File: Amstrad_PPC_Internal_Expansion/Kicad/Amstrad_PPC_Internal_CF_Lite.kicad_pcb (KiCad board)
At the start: 2 copper layers, 120 x 205 mm, 36 parts, among them J1 Amstrad_PPC_ISA_Connector_B, J2 Amstrad_PPC_ISA_Connector_A, J3 CONN_CF_CARD, J4 Conn_01x02, SW1 Switch_DIP_4_Positions, SW2 Switch_DIP_8_Positions, U1 74HCT244, U2 74HCT244, U3 74HCT688, U4 74LS32, U5 74HCT04, U6 74HCT688, U7 28C256

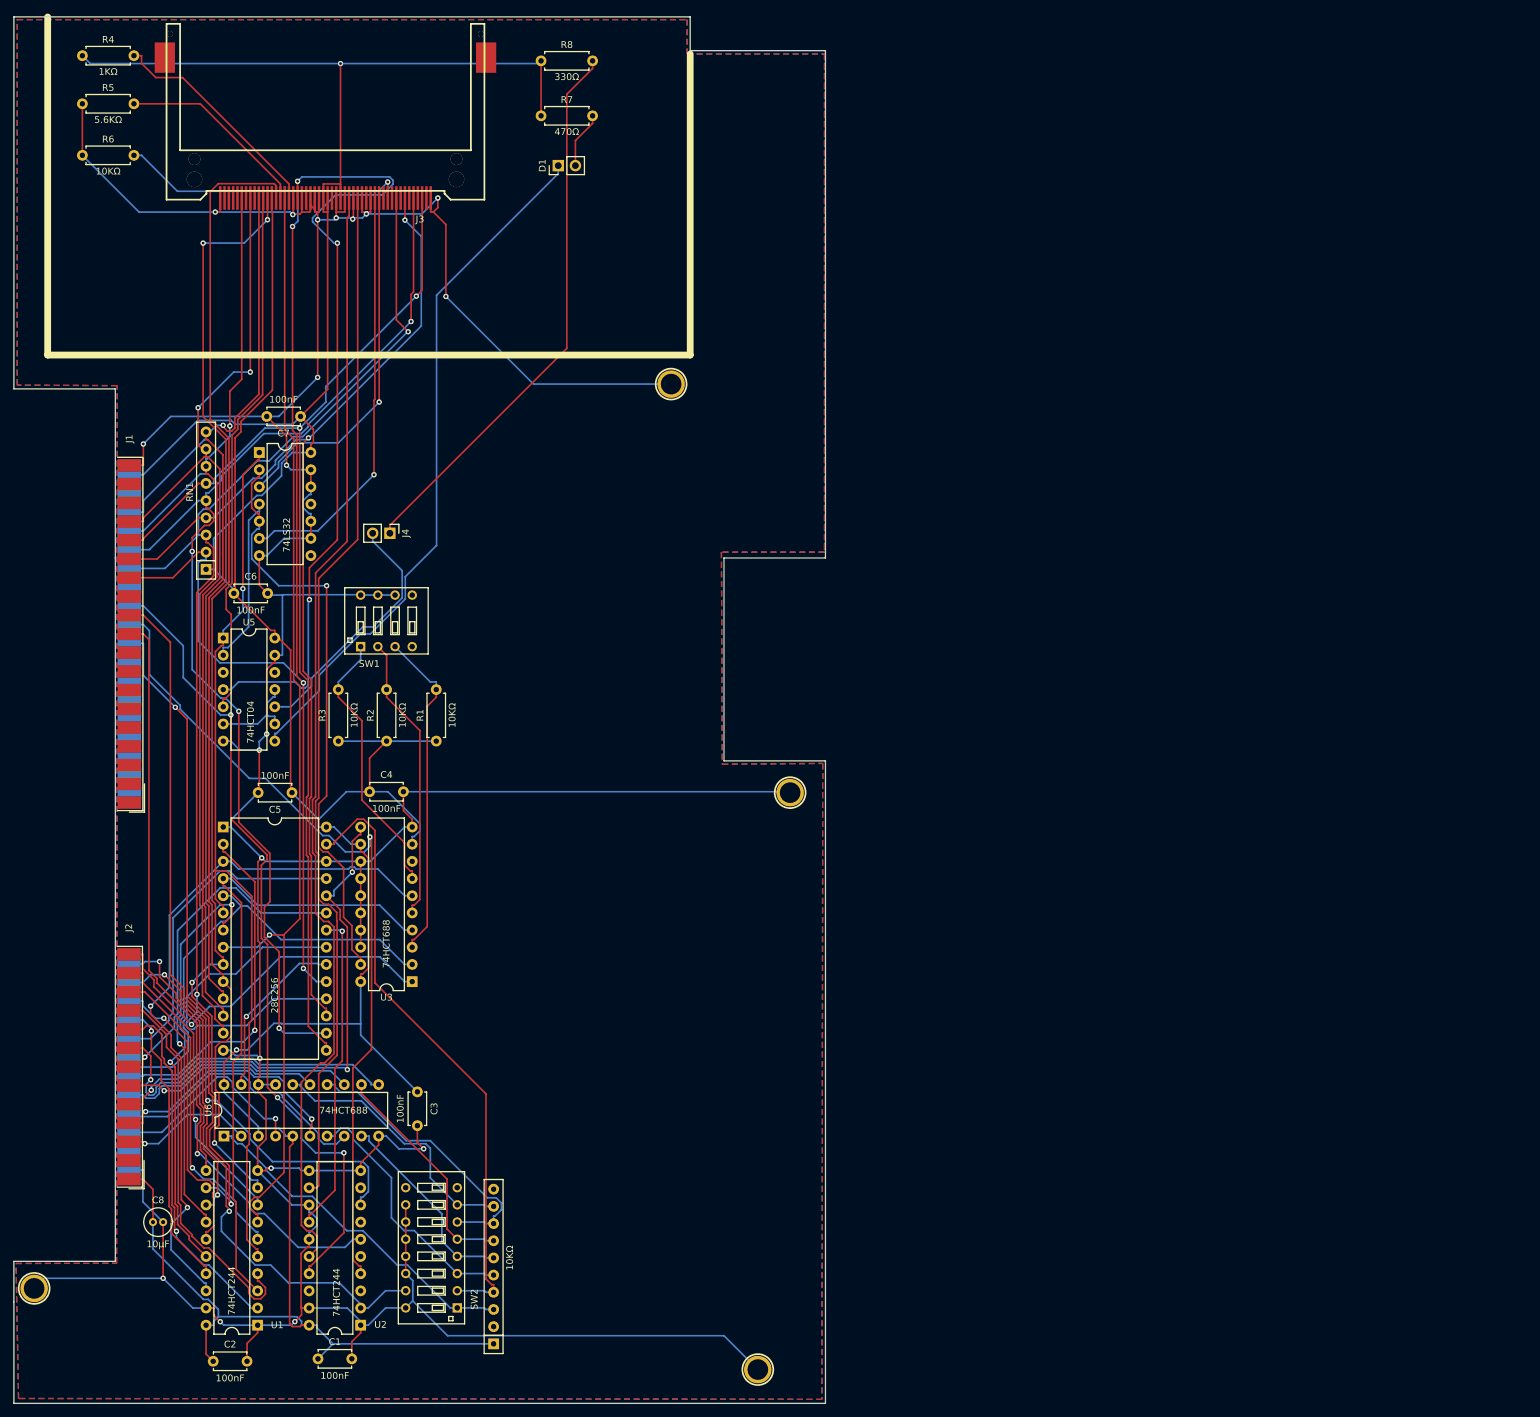
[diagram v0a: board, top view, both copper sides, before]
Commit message: Starting again ... initial schematic cleanup
Schematic is now cleaned up, no errors
Next will be PCB layout
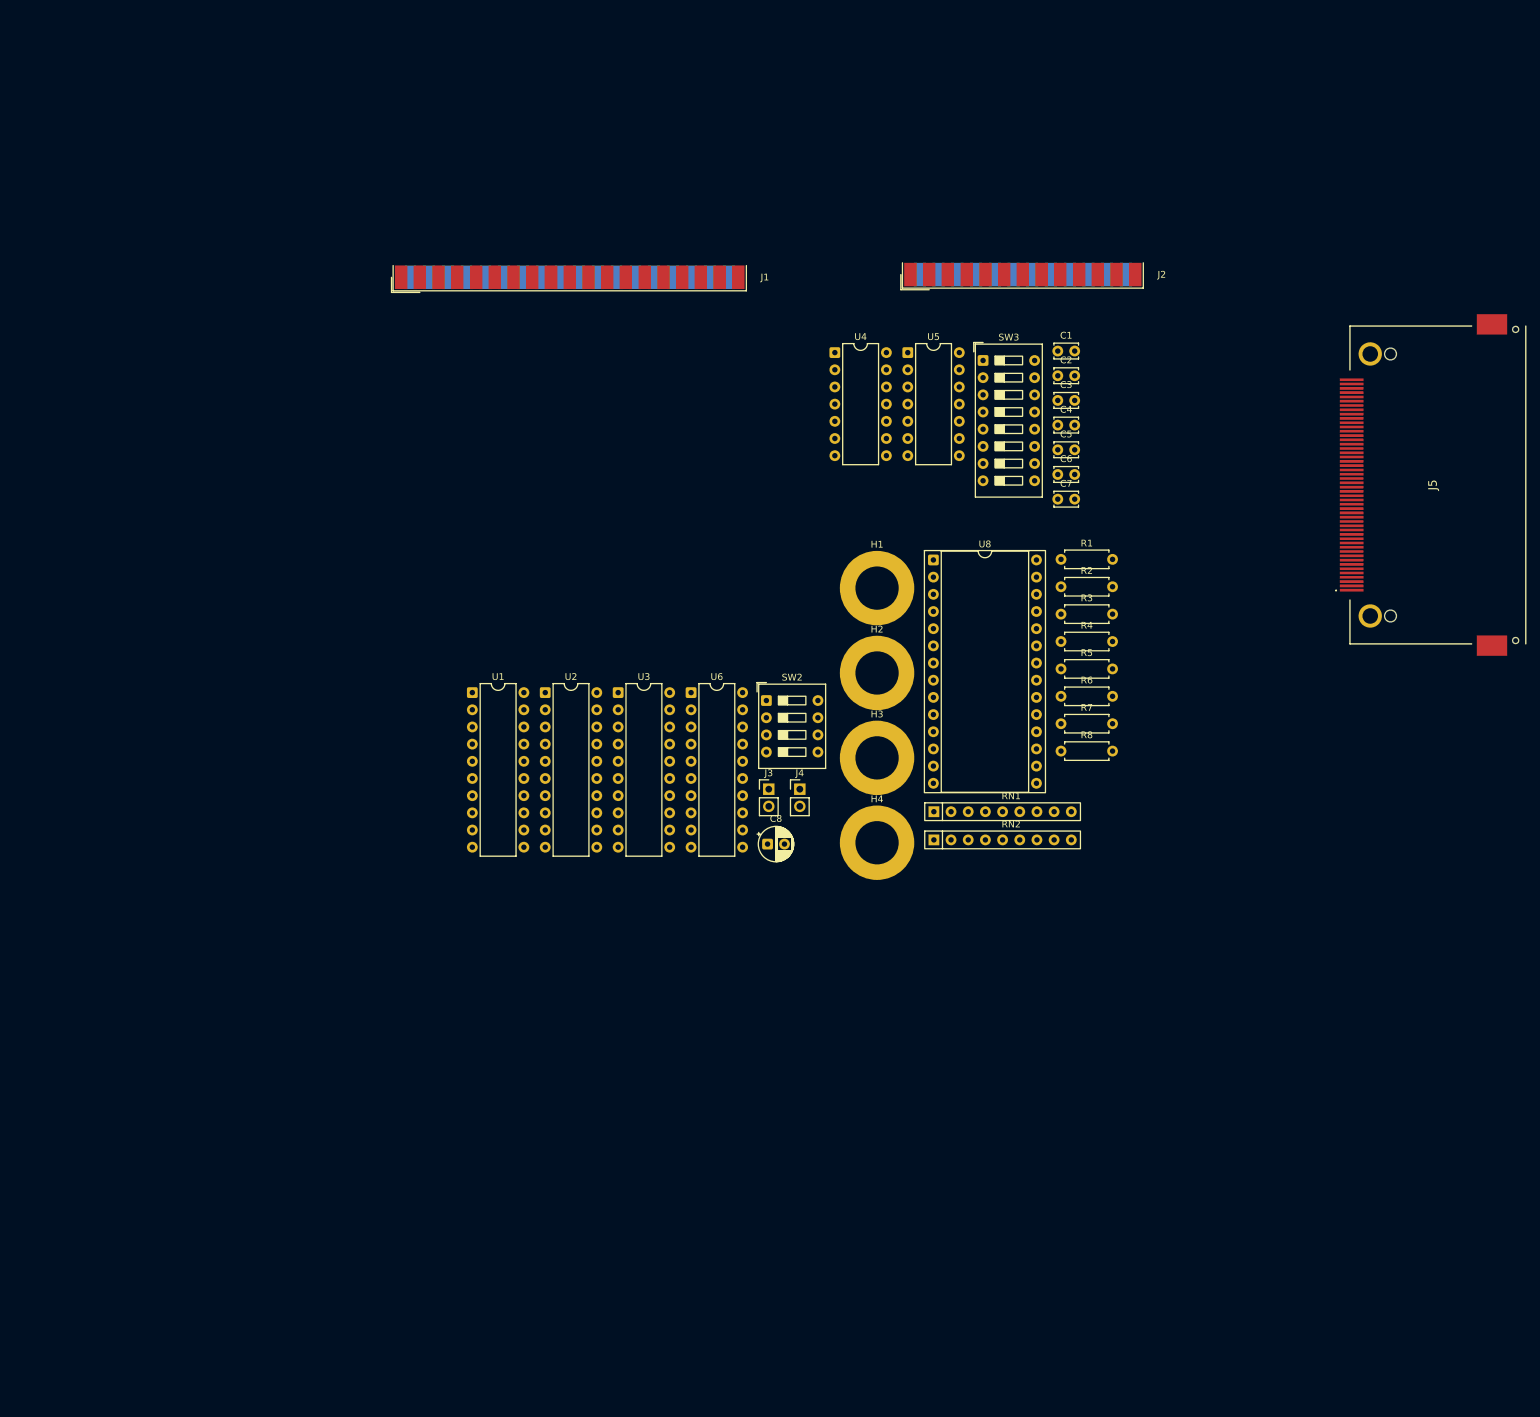
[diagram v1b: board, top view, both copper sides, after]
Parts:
- removed D1: LED, Connector_PinHeader_2.54mm:PinHeader_1x02_P2.54mm_Vertical
- removed HOLE1, HOLE2, HOLE3, HOLE4: HOLE, My_Components:Hole_3mm
- removed RR1: 10KΩ, Resistor_THT:R_Array_SIP10
- removed SW1: Switch_DIP_4_Positions, My_Components:Switch_DIP_4_Positions
- removed U7: 28C256, Package_DIP:DIP-28_W15.24mm
- added H1: MountingHole_Pad, MountingHole:MountingHole_6.4mm_M6_DIN965_Pad, F.Cu at (157.6, 109.5)
- added H2: MountingHole_Pad, MountingHole:MountingHole_6.4mm_M6_DIN965_Pad, F.Cu at (157.6, 122.0)
- added H3: MountingHole_Pad, MountingHole:MountingHole_6.4mm_M6_DIN965_Pad, F.Cu at (157.6, 134.6)
- added H4: MountingHole_Pad, MountingHole:MountingHole_6.4mm_M6_DIN965_Pad, F.Cu at (157.6, 147.1)
- added J5: N7E50-Q516RB-50-WF, Amstrad_PPC:N7E50Q516RB50WF, F.Cu at (240.6, 94.2)
- added RN2: 10KΩ, Resistor_THT:R_Array_SIP9, F.Cu at (166.0, 146.7)
- added SW3: SW_DIP_x08, Button_Switch_THT:SW_DIP_SPSTx08_Slide_9.78x22.5mm_W7.62mm_P2.54mm, F.Cu at (173.3, 75.8)
- added U8: 28C256, Package_DIP:DIP-28_W15.24mm_Socket, F.Cu at (166.0, 105.3)
- C1, C2, C3, C4, C5, C6, C7: footprint Capacitor_THT:C_Disc_D4.7mm_W2.5mm_P5.00mm -> Capacitor_THT:C_Disc_D3.4mm_W2.1mm_P2.50mm
- C8: footprint Capacitor_THT:C_Radial_D4.0mm_H5.0mm_P1.50mm -> Capacitor_THT:CP_Radial_D5.0mm_P2.50mm
- J1: footprint Connector_Dsub:DSUB-37_Female_EdgeMount_P2.77mm -> Connector_Dsub:DSUB-37_Socket_EdgeMount_P2.77mm
- J2: footprint Connector_Dsub:DSUB-25_Female_EdgeMount_P2.77mm -> Connector_Dsub:DSUB-25_Socket_EdgeMount_P2.77mm
- J3: value CONN_CF_CARD -> LED; footprint My_Components:Conn_CF_N7E50-Q516XX-40 -> Connector_PinHeader_2.54mm:PinHeader_1x02_P2.54mm_Vertical
- J4: value Conn_01x02 -> LED
- SW2: value Switch_DIP_8_Positions -> SW_DIP_x04; footprint My_Components:Switch_DIP_8_Positions -> Button_Switch_THT:SW_DIP_SPSTx04_Slide_9.78x12.34mm_W7.62mm_P2.54mm
- U4: value 74LS32 -> 74HCT32
- moved C2 191.9 mm to (184.3, 78.1)
- moved C1 184.8 mm to (184.3, 74.4)
- moved J2 176.6 mm to (179.2, 63.1), turned to 180 degrees
- moved R4 168.6 mm to (184.8, 117.4)
- moved R5 167.1 mm to (184.8, 121.4)
- moved R6 165.3 mm to (184.8, 125.5)
- moved C3 139.3 mm to (184.3, 81.7), turned to 0 degrees
- moved R8 127.8 mm to (184.8, 133.6)
- moved C5 124.1 mm to (184.3, 89.0), turned to 0 degrees
- moved C6 123.1 mm to (184.3, 92.7)
- moved R7 118.3 mm to (184.8, 129.5)
- moved C4 115.3 mm to (184.3, 85.4)
- moved J3 113.9 mm to (141.6, 139.2), turned to 0 degrees
- moved RN1 113.4 mm to (166.0, 142.5), turned to 0 degrees
- moved C7 112.6 mm to (184.3, 96.3), turned to 0 degrees
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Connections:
- net /A09 renamed /A_{09}
- net /A13 renamed /A_{13}
- net /A14 renamed /A_{14}
- net /A15 renamed /A_{15}
- net /A16 renamed /A_{16}
- net /A17 renamed /A_{17}
- net /A18 renamed /A_{18}
- net /A19 renamed /A_{19}
- J1 pad 13: /D7 -> /D_{7}
- J1 pad 14: /D5 -> /D_{5}
- J1 pad 15: /D3 -> /D_{3}
- J1 pad 16: /D1 -> /D_{1}
- J1 pad 32: /D6 -> /D_{6}
- J1 pad 33: /D4 -> /D_{4}
- J1 pad 34: /D2 -> /D_{2}
- J1 pad 35: /D0 -> /D_{0}
- J2 pad 10: /A05 -> /A_{05}
- J2 pad 11: /A03 -> /A_{03}
- J2 pad 12: /A01 -> /A_{01}
- J2 pad 19: /A12 -> /A_{12}
- J2 pad 20: /A10 -> /A_{10}
- J2 pad 21: /A08 -> /A_{08}
- J2 pad 22: /A06 -> /A_{06}
- J2 pad 23: /A04 -> /A_{04}
- J2 pad 24: /A02 -> /A_{02}
- J2 pad 25: /A00 -> /A_{00}
- J2 pad 7: /A11 -> /A_{11}
- J2 pad 9: /A07 -> /A_{07}
- J3 pad 1: GND -> Net-(J3-Pin_1)
- J3 pad 2: /D3 -> Net-(J3-Pin_2)
- R5 pad 1: GND -> /CF_DMARQ
- R5 pad 2: /CF_DMARQ -> GND
- R6 pad 2: /D7 -> /D_{7}
- R7 pad 2: Net-(D1-A) -> Net-(J3-Pin_1)
- RN1 pad 2: /D7 -> /D_{7}
- RN1 pad 3: /D6 -> /D_{6}
- RN1 pad 4: /D5 -> /D_{5}
- RN1 pad 5: /D4 -> /D_{4}
- RN1 pad 6: /D3 -> /D_{3}
- RN1 pad 7: /D2 -> /D_{2}
- RN1 pad 8: /D1 -> /D_{1}
- RN1 pad 9: /D0 -> /D_{0}
- SW2 pad 1: Net-(U6-G) -> Net-(U3-R2)
- SW2 pad 2: /~{ROMW} -> Net-(U3-R1)
- SW2 pad 3: Net-(U6-R2) -> Net-(U3-R0)
- SW2 pad 4: Net-(U6-R3) -> unconnected-(SW2-Pad4)
- SW2 pad 5: Net-(U6-R4) -> unconnected-(SW2-Pad5)
- SW2 pad 6: Net-(U6-R5) -> GND
- SW2 pad 7: Net-(U6-R6) -> GND
- SW2 pad 8: unconnected-(SW2-Pad8) -> GND
- U1 pad 11: /A00 -> /A_{07}
- U1 pad 12: /B_A01 -> /B_A_{03}
- U1 pad 13: /A02 -> /A_{06}
- U1 pad 14: /B_A03 -> /B_A_{02}
- U1 pad 15: /A04 -> /A_{05}
- U1 pad 16: /B_A05 -> /B_A_{01}
- U1 pad 17: /A06 -> /A_{04}
- U1 pad 18: /B_A07 -> /B_A_{00}
- U1 pad 2: /A07 -> /A_{00}
- U1 pad 3: /B_A06 -> /B_A_{04}
- U1 pad 4: /A05 -> /A_{01}
- U1 pad 5: /B_A04 -> /B_A_{05}
- U1 pad 6: /A03 -> /A_{02}
- U1 pad 7: /B_A02 -> /B_A_{06}
- U1 pad 8: /A01 -> /A_{03}
- U1 pad 9: /B_A00 -> /B_A_{07}
- U3 pad 2: /B_A05 -> /B_A_{05}
- U3 pad 4: /B_A06 -> /B_A_{06}
- U3 pad 6: /B_A07 -> /B_A_{07}
- U3 pad 8: /B_A08 -> /A_{08}
- U4 pad 1: /B_A04 -> /B_A_{04}
- U5 pad 1: /B_A04 -> /B_A_{04}
- U5 pad 3: unconnected-(U5-Pad3) -> /B_RESET
- U5 pad 4: /~{CF_RESET} -> /~{B_RESET}
- U5 pad 8: Net-(D1-K) -> Net-(J3-Pin_2)
- U6 pad 1: Net-(U6-G) -> Net-(RN2-R1)
- U6 pad 12: Net-(U6-R4) -> Net-(RN2-R5)
- U6 pad 14: Net-(U6-R5) -> Net-(RN2-R6)
- U6 pad 16: Net-(U6-R6) -> Net-(RN2-R7)
- U6 pad 7: Net-(U6-R2) -> Net-(RN2-R3)
- U6 pad 9: Net-(U6-R3) -> Net-(RN2-R4)
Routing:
- net GND: track 702.2 -> 0.00 mm, vias 20 -> 0
- net VCC: track 554.3 -> 0.00 mm, vias 2 -> 0
- net /D7: track 207.8 -> 0.00 mm, vias 4 -> 0
- net /D6: track 176.8 -> 0.00 mm, vias 2 -> 0
- net /B_A01: track 176.0 -> 0.00 mm, vias 2 -> 0
- net /D4: track 169.3 -> 0.00 mm, vias 4 -> 0
- net /D3: track 168.1 -> 0.00 mm, vias 2 -> 0
- net /B_A02: track 166.1 -> 0.00 mm, vias 1 -> 0
- net /D5: track 165.3 -> 0.00 mm, vias 2 -> 0
- net /~{B_IOW}: track 164.6 -> 0.00 mm
- net /B_A00: track 162.8 -> 0.00 mm, vias 3 -> 0
- net /~{B_IOR}: track 153.0 -> 0.00 mm
- net /D0: track 146.2 -> 0.00 mm, vias 1 -> 0
- net /D1: track 145.6 -> 0.00 mm, vias 2 -> 0
- net /D2: track 145.2 -> 0.00 mm, vias 1 -> 0
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- removed copper zone on B.Cu, net GND
- removed copper zone on F.Cu, net GND
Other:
- board outline removed

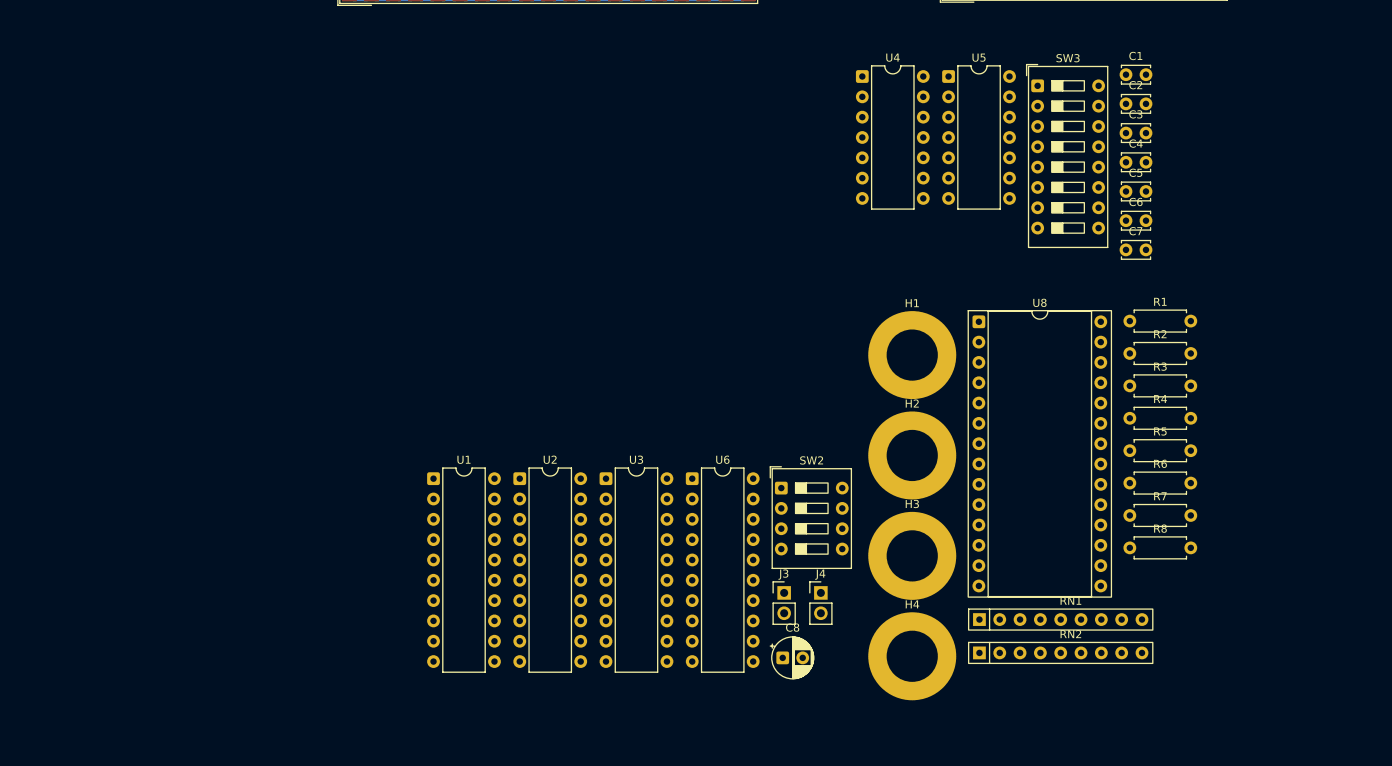
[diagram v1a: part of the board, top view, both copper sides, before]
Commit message: Update Amstrad_PPC_Internal_CF_Lite.kicad_pcb
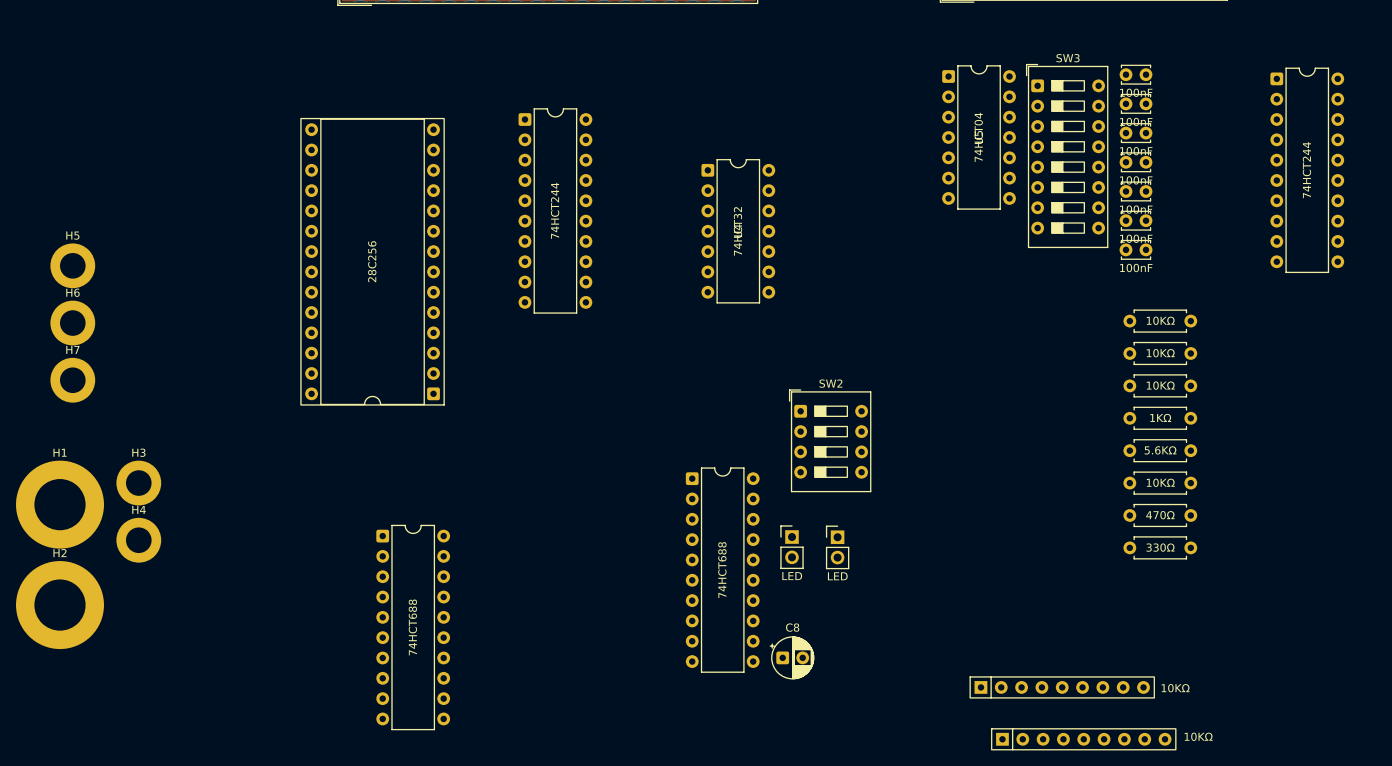
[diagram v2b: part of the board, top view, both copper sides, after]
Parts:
- added H5: MountingHole_Pad, MountingHole:MountingHole_3.2mm_M3_DIN965_Pad, F.Cu at (52.7, 98.3)
- added H6: MountingHole_Pad, MountingHole:MountingHole_3.2mm_M3_DIN965_Pad, F.Cu at (52.7, 105.5)
- added H7: MountingHole_Pad, MountingHole:MountingHole_3.2mm_M3_DIN965_Pad, F.Cu at (52.7, 112.6)
- H3, H4: footprint MountingHole:MountingHole_6.4mm_M6_DIN965_Pad -> MountingHole:MountingHole_3.2mm_M3_DIN965_Pad
- moved U1 116.7 mm to (203.2, 74.9)
- moved H1 108.2 mm to (51.1, 128.2)
- moved H2 108.2 mm to (51.1, 140.7)
- moved H4 97.8 mm to (61.0, 132.6)
- moved H3 97.1 mm to (61.0, 125.5)
- moved U8 68.8 mm to (97.8, 114.3), turned to 180 degrees
- moved U2 44.9 mm to (109.2, 80.0)
- moved U3 28.8 mm to (91.4, 132.1)
- moved U4 22.6 mm to (132.1, 86.4)
- moved RN1 15.2 mm to (168.9, 157.5)
- moved SW2 9.90 mm to (143.7, 116.5)
- moved J4 7.27 mm to (148.3, 132.2)
- moved J3 7.05 mm to (142.6, 132.2)
- moved RN2 4.32 mm to (166.2, 151.0)
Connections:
- SW3 pad 2: /~{MEMW} -> /~{B_MEMW}
